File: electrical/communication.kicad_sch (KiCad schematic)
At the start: 9 parts

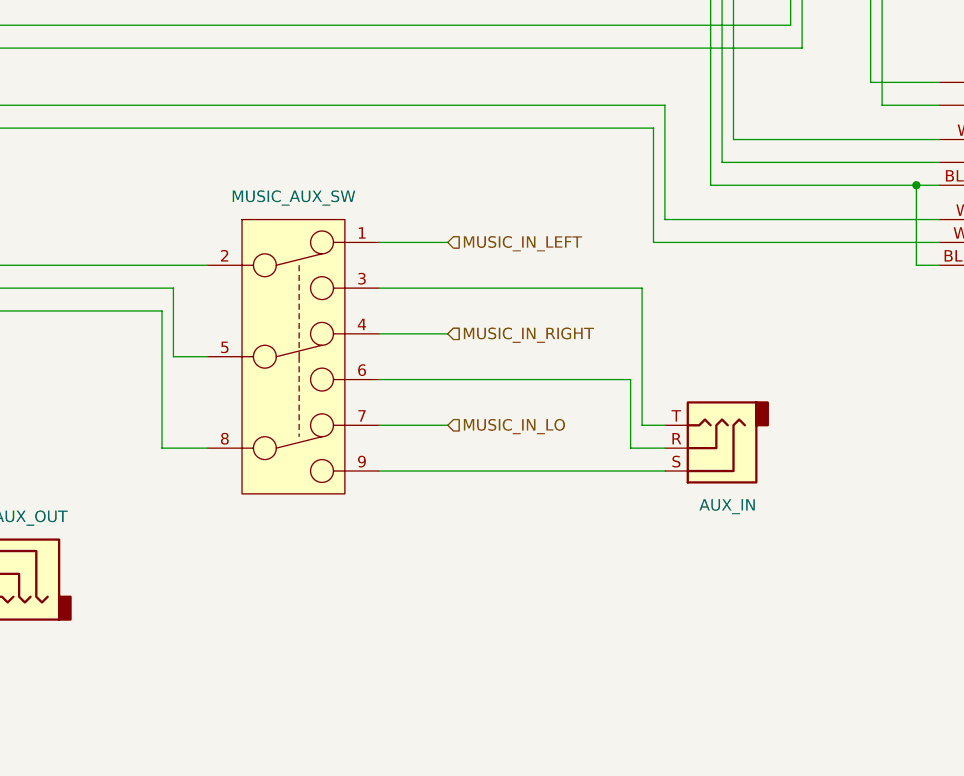
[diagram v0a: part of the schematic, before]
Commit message: Added bluetooth
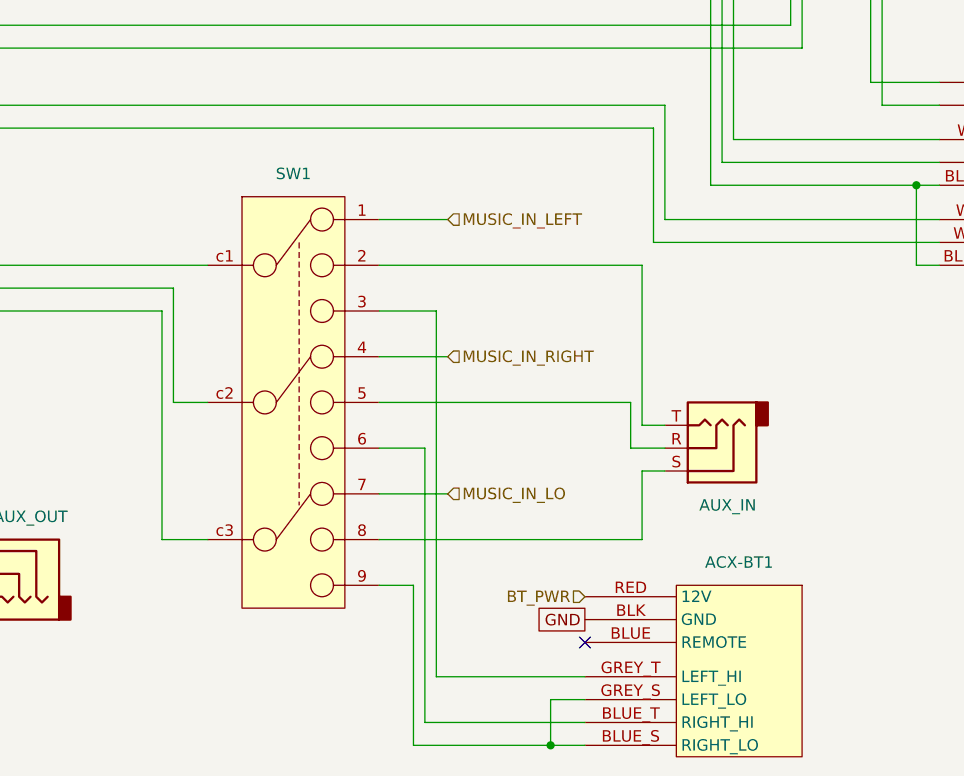
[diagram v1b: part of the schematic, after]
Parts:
- removed MUSIC_AUX_SW: ~, symbol flyerx:SW_3PDT_Toggle
- added ACX-BT1: ~, symbol flyerx:AudioControl_ACX-BT1
- added SW1: ~, symbol flyerx:SW_3P3T_Rotary
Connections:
- net GND: now also ACX-BT1.BLK (GND)
- net MUSIC_IN_LEFT: now also SW1.1
- net MUSIC_IN_LO: now also SW1.7
- net MUSIC_IN_RIGHT: now also SW1.4
- net at AUX_IN.R: now also SW1.5
- net at AUX_IN.S: now also SW1.8
- net at AUX_IN.T: now also SW1.2
- net at GTR20.P2001_19 (MUSIC_IN_LEFT): now also SW1.c1
- net at GTR20.P2001_18 (MUSIC_IN_RIGHT): now also SW1.c2
- net at GTR20.P2001_37 (MUSIC_LO): now also SW1.c3
- new net: ACX-BT1.GREY_T (LEFT_HI), SW1.3
- new net: ACX-BT1.BLUE_T (RIGHT_HI), SW1.6
- new net: ACX-BT1.BLUE_S (RIGHT_LO), ACX-BT1.GREY_S (LEFT_LO), SW1.9
- new net BT_PWR: ACX-BT1.RED (12V)
- no-connect marks 0 -> 1

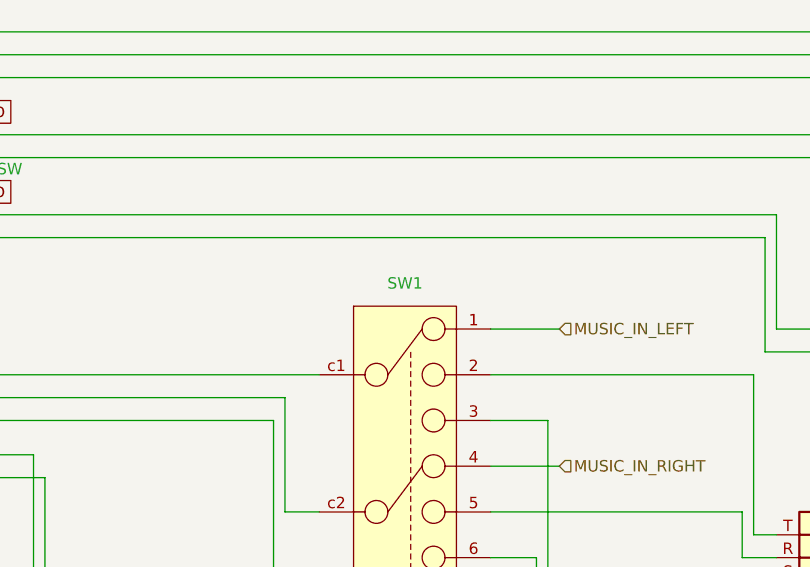
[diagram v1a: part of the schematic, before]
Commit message: Converted to breakers w/GAD 27 instead of VP-X.
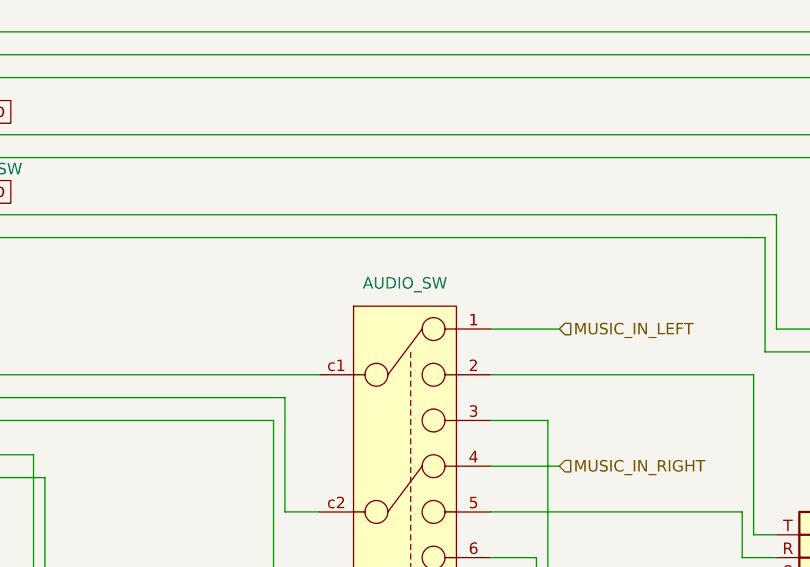
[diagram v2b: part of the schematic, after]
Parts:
- renumbered SW1 to AUDIO_SW
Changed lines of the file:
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@@
     (title "Communication")
     (date "2024-03-15")
-    (rev "0.9.2")
+    (rev "1.0")
     (company "N915SN Angry Bird")
+    (comment 1 "w/Breakers")
   )
   (junction (at 81.28 44.45) (diameter 0) (color 0 0 0 0)
@@
   (symbol (lib_id "flyerx:SW_3P3T_Rotary") (at 148.59 107.95 0) (unit 1)
     (in_bom yes) (on_board yes) (dnp no) (fields_autoplaced)
-    (property "Reference" "SW1" (at 147.955 105.41 0)
+    (property "Reference" "AUDIO_SW" (at 147.955 105.41 0)
       (effects (font (size 1.27 1.27)))
     )
@@
       (project "electrical"
         (path "/e8ec215a-dbe2-4eba-a577-e50a0a128049/facdf550-4f2c-4387-974e-24c6900d900d"
-          (reference "SW1") (unit 1)
+          (reference "AUDIO_SW") (unit 1)
         )
       )

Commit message: Interim check-in. Not sure what I was doing.
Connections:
- net CAN_HI_IN: now also GTR20.P2001_7 (CAN_BUS_HI); no longer GTR20.P2001_8 (ID_IN)
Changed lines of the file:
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@@
     (stroke (width 0) (type default))
+  )
+  (text_box "GTR20\n 1 Power\n 6 Can Bus Lo\n 7 Can Bus Hi\n10 Receiver Audio Out Hi\n11 Copilot HS Right\n12 Copilot HS Left\n13 Pilot HS Right\n14 Pilot HS Left\n15 Copilot PTT\n16 Copilot Mic In\n17 Pilot Mic In\n18 Music In Right\n19 Music In Left\n20 Ground\n29 Receiver Audio Lo\n30 Copilot hs Lo\n31 Aux 1 Lo\n32 Aux Mono In 1\n33 Pilot HS Lo\n34 Copilot Mic Lo\n35 Pilot PTT\n36 Pilot Mic Lo\n37 Music Lo"
+    (at 127 13.97 0) (size 27.305 50.8)
+    (stroke (width 0) (type default))
+    (fill (type none))
+    (effects (font (size 1.27 1.27)) (justify left top))
   )
   (global_label "GND" (shape passive) (at 99.06 95.25 0) (fields_autoplaced)
@@
     (pin "P2001_6")
     (pin "P2001_8")
-    (pin "P2001_8")
+    (pin "P2001_7")
     (pin "P2001_9")
     (instances

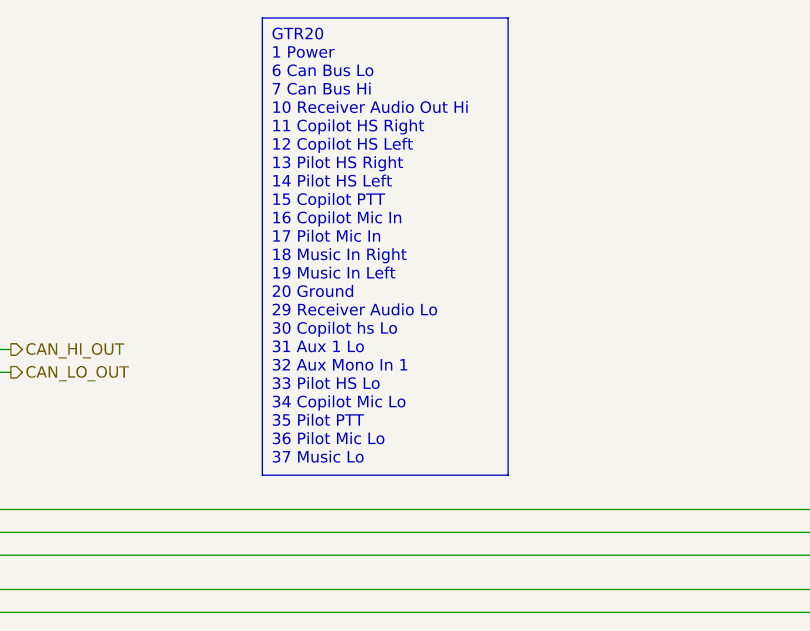
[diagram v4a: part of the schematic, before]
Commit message: Cleaned up power and smoke.
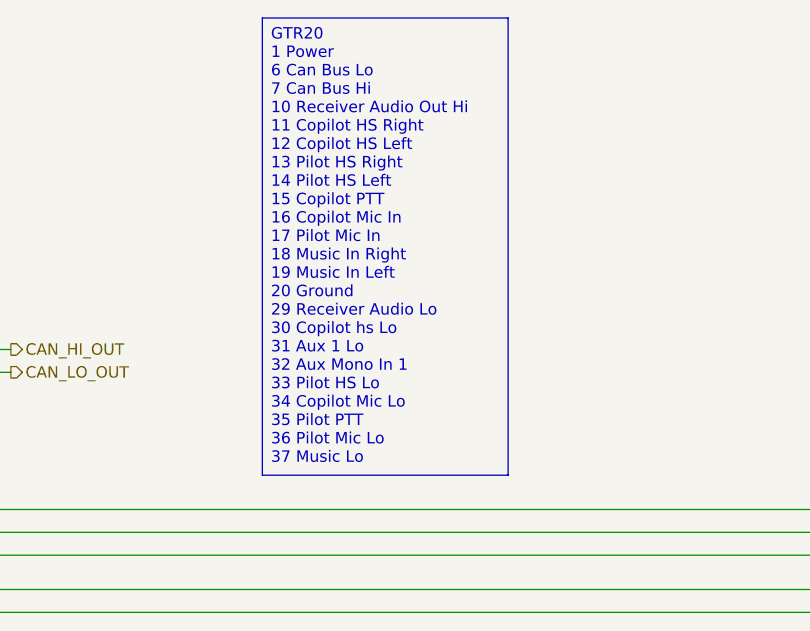
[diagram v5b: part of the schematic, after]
